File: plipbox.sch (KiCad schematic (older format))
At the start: 10 parts, among them P1 PWR, P2 PARALLEL_PORT, P3 RS232, U1 MAX3221, U2 ARDUINO_NANO_V3

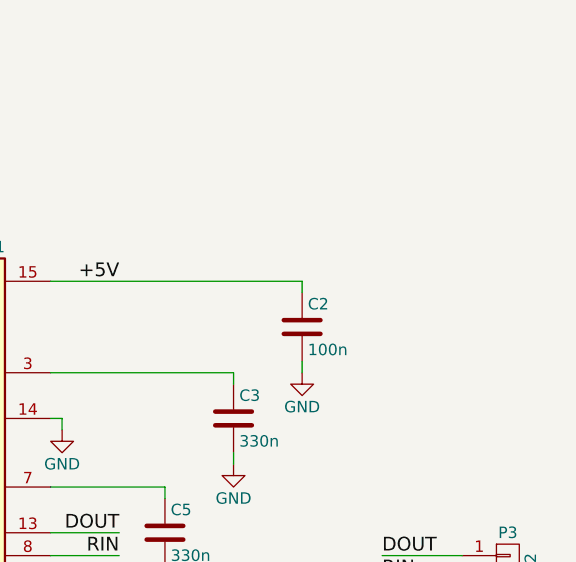
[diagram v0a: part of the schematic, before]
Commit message: ERC power flag errors
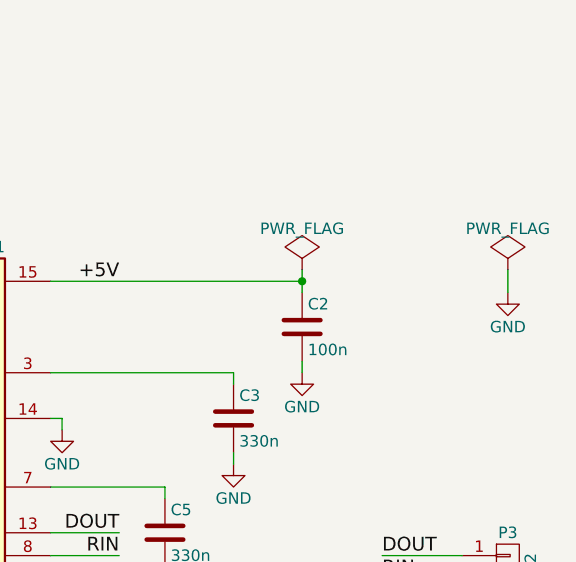
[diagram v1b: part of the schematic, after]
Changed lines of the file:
@@
 $EndComp
 Wire Wire Line
-	9700 2100 9700 2150
+	9700 2050 9700 2150
 Wire Wire Line
 	9700 2450 9700 2500
@@
 Wire Wire Line
 	4850 4400 4850 4450
+$Comp
+L PWR_FLAG #FLG012
+U 1 1 59594524
+P 9700 2050
+F 0 "#FLG012" H 9700 2145 50  0001 C CNN
+F 1 "PWR_FLAG" H 9700 2230 50  0000 C CNN
+F 2 "" H 9700 2050 50  0000 C CNN
+F 3 "" H 9700 2050 50  0000 C CNN
+	1    9700 2050
+	1    0    0    -1
+$EndComp
+Connection ~ 9700 2100
+$Comp
+L GND #PWR013
+U 1 1 59594637
+P 10600 2150
+F 0 "#PWR013" H 10600 1900 50  0001 C CNN
+F 1 "GND" H 10600 2000 50  0000 C CNN
+F 2 "" H 10600 2150 50  0000 C CNN
+F 3 "" H 10600 2150 50  0000 C CNN
+	1    10600 2150
+	1    0    0    -1
+$EndComp
+$Comp
+L PWR_FLAG #FLG014
+U 1 1 59594912
+P 10600 2050
+F 0 "#FLG014" H 10600 2145 50  0001 C CNN
+F 1 "PWR_FLAG" H 10600 2230 50  0000 C CNN
+F 2 "" H 10600 2050 50  0000 C CNN
+F 3 "" H 10600 2050 50  0000 C CNN
+	1    10600 2050
+	1    0    0    -1
+$EndComp
+Wire Wire Line
+	10600 2050 10600 2150
 $EndSCHEMATC
